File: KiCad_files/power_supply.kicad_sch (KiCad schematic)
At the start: 24 parts, among them Q2 DMP3099L, SW1 SLW-171175-7A-N-D, U7 LTC4412xS6

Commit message: comments
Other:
- note added: "Bootstrapping diode recommended by datasheet, since duty cycle expected be > 65% when powered through USB"
- note added: "DPDT switch because DPST switches with our power requirements were very expensive"
- note added: "Extra pad so that extra capacitor can be added if needed"
- note added: "Power LED"
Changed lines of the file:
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@@
 	(generator_version "9.0")
 	(paper "A4")
+	(text "Extra pad so that extra capacitor can be added if needed"
+		(exclude_from_sim no)
+		(at 198.374 123.19 0)
+		(effects
+			(font
+				(size 1.27 1.27)
+			)
+		)
+	)
 	(text "Power flags everywhere to tell ERC to STFU"
 		(exclude_from_sim no)
@@
 		(effects
 			(font
+				(size 1.27 1.27)
+			)
+		)
+	)
+	(text "Power LED"
+		(exclude_from_sim no)
+		(at 272.288 75.946 0)
+		(effects
+			(font
+				(size 1.27 1.27)
+			)
+		)
+	)
+	(text "Bootstrapping diode recommended by datasheet, since duty cycle expected be > 65% when powered through USB"
+		(exclude_from_sim no)
+		(at 192.278 31.242 0)
+		(effects
+			(font
+				(size 1.27 1.27)
+			)
+		)
+	)
+	(text "DPDT switch because DPST switches with our power requirements were very expensive"
+		(exclude_from_sim no)
+		(at 57.658 77.978 0)
+		(effects
+			(font

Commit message: more comments
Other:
- note added: "C25 and C26 are extra pad so that extra capacitor can be added if needed"
- note added: "LTC4412 is ideal diode. Uses reference design from datasheet"
- note added: "MP2235S is switching regulator (buck converter)"
- note added: "R11, C18, C19 and D3 form bootstrapping circuitry. 1n4148 diode recommended by datasheet when dutycycle > 65%"
- note added: "R12, R13, R14, C21 form feedback circuitry. From MPS DCDC-Designer tool"
- note added: "R15 is pullup resistor for BAT_STAT. LTC4412 pull down when current flows from USB"
- note added: "SW1 is power switch. Turns power on/off from both input power sources (USB and battery)"
- note removed: "Bootstrapping diode recommended by datasheet, since duty cycle expected be > 65% when powered through USB"
- note removed: "Extra pad so that extra capacitor can be added if needed"
- note removed: "Power flags everywhere to tell ERC to STFU"
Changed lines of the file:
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@@
 	(generator_version "9.0")
 	(paper "A4")
-	(text "Extra pad so that extra capacitor can be added if needed"
+	(text "C25 and C26 are extra pad so that extra capacitor can be added if needed"
 		(exclude_from_sim no)
-		(at 198.374 123.19 0)
+		(at 162.814 109.982 0)
 		(effects
 			(font
@@
 		)
 	)
-	(text "Power flags everywhere to tell ERC to STFU"
+	(text "SW1 is power switch. Turns power on/off from both input power sources (USB and battery)"
 		(exclude_from_sim no)
-		(at 68.58 69.596 0)
+		(at 58.166 53.848 0)
+		(effects
+			(font
+				(size 1.27 1.27)
+			)
+		)
+	)
+	(text "R12, R13, R14, C21 form feedback circuitry. From MPS DCDC-Designer tool"
+		(exclude_from_sim no)
+		(at 239.014 41.148 0)
+		(effects
+			(font
+				(size 1.27 1.27)
+			)
+		)
+	)
+	(text "R11, C18, C19 and D3 form bootstrapping circuitry. 1n4148 diode recommended by datasheet when dutycycle > 65%"
+		(exclude_from_sim no)
+		(at 166.37 32.766 0)
 		(effects
 			(font
@@
 		)
 	)
-	(text "Bootstrapping diode recommended by datasheet, since duty cycle expected be > 65% when powered through USB"
+	(text "R15 is pullup resistor for BAT_STAT. LTC4412 pull down when current flows from USB"
+		(exclude_from_sim no)
+		(at 235.712 148.082 0)
+		(effects
+			(font
+				(size 1.27 1.27)
+			)
+		)
+	)
+	(text "LTC4412 is ideal diode. Uses reference design from datasheet"
 		(exclude_from_sim no)
-		(at 192.278 31.242 0)
+		(at 67.564 164.846 0)
+		(effects
+			(font
+				(size 1.27 1.27)
+			)
+		)
+	)
+	(text "MP2235S is switching regulator (buck converter)"
+		(exclude_from_sim no)
+		(at 138.938 18.796 0)
 		(effects
 			(font
@@
 	(text "DPDT switch because DPST switches with our power requirements were very expensive"
 		(exclude_from_sim no)
-		(at 57.658 77.978 0)
+		(at 55.626 60.198 0)
 		(effects
 			(font
@@
 		)
 		(instances
-			(project ""
+			(project "esp"
 				(path "/186d5500-054c-4b47-a89c-85f6ce2abe33/718dca9f-314d-4628-afec-7956f3606013"
 					(reference "D1")
@@
 		)
 		(instances
-			(project ""
+			(project "esp"
 				(path "/186d5500-054c-4b47-a89c-85f6ce2abe33/718dca9f-314d-4628-afec-7956f3606013"
 					(reference "#PWR01")
@@
 		)
 		(instances
-			(project ""
+			(project "esp"
 				(path "/186d5500-054c-4b47-a89c-85f6ce2abe33/718dca9f-314d-4628-afec-7956f3606013"
 					(reference "#FLG04")
@@
 		)
 		(instances
-			(project ""
+			(project "esp"
 				(path "/186d5500-054c-4b47-a89c-85f6ce2abe33/718dca9f-314d-4628-afec-7956f3606013"
 					(reference "C20")
@@
 		)
 		(instances
-			(project ""
+			(project "esp"
 				(path "/186d5500-054c-4b47-a89c-85f6ce2abe33/718dca9f-314d-4628-afec-7956f3606013"
 					(reference "C21")
@@
 		)
 		(instances
-			(project ""
+			(project "esp"
 				(path "/186d5500-054c-4b47-a89c-85f6ce2abe33/718dca9f-314d-4628-afec-7956f3606013"
 					(reference "R15")
@@
 		)
 		(instances
-			(project ""
+			(project "esp"
 				(path "/186d5500-054c-4b47-a89c-85f6ce2abe33/718dca9f-314d-4628-afec-7956f3606013"
 					(reference "R1")
@@
 		)
 		(instances
-			(project ""
+			(project "esp"
 				(path "/186d5500-054c-4b47-a89c-85f6ce2abe33/718dca9f-314d-4628-afec-7956f3606013"
 					(reference "L4")
@@
 		)
 		(instances
-			(project ""
+			(project "esp"
 				(path "/186d5500-054c-4b47-a89c-85f6ce2abe33/718dca9f-314d-4628-afec-7956f3606013"
 					(reference "D3")
@@
 		)
 		(instances
-			(project ""
+			(project "esp"
 				(path "/186d5500-054c-4b47-a89c-85f6ce2abe33/718dca9f-314d-4628-afec-7956f3606013"
 					(reference "#PWR052")
@@
 		)
 		(instances
-			(project ""
+			(project "esp"
 				(path "/186d5500-054c-4b47-a89c-85f6ce2abe33/718dca9f-314d-4628-afec-7956f3606013"
 					(reference "#FLG07")
@@
 		)
 		(instances
-			(project ""
+			(project "esp"
 				(path "/186d5500-054c-4b47-a89c-85f6ce2abe33/718dca9f-314d-4628-afec-7956f3606013"
 					(reference "#PWR020")
@@
 		)
 		(instances
-			(project ""
+			(project "esp"
 				(path "/186d5500-054c-4b47-a89c-85f6ce2abe33/718dca9f-314d-4628-afec-7956f3606013"
 					(reference "SW1")

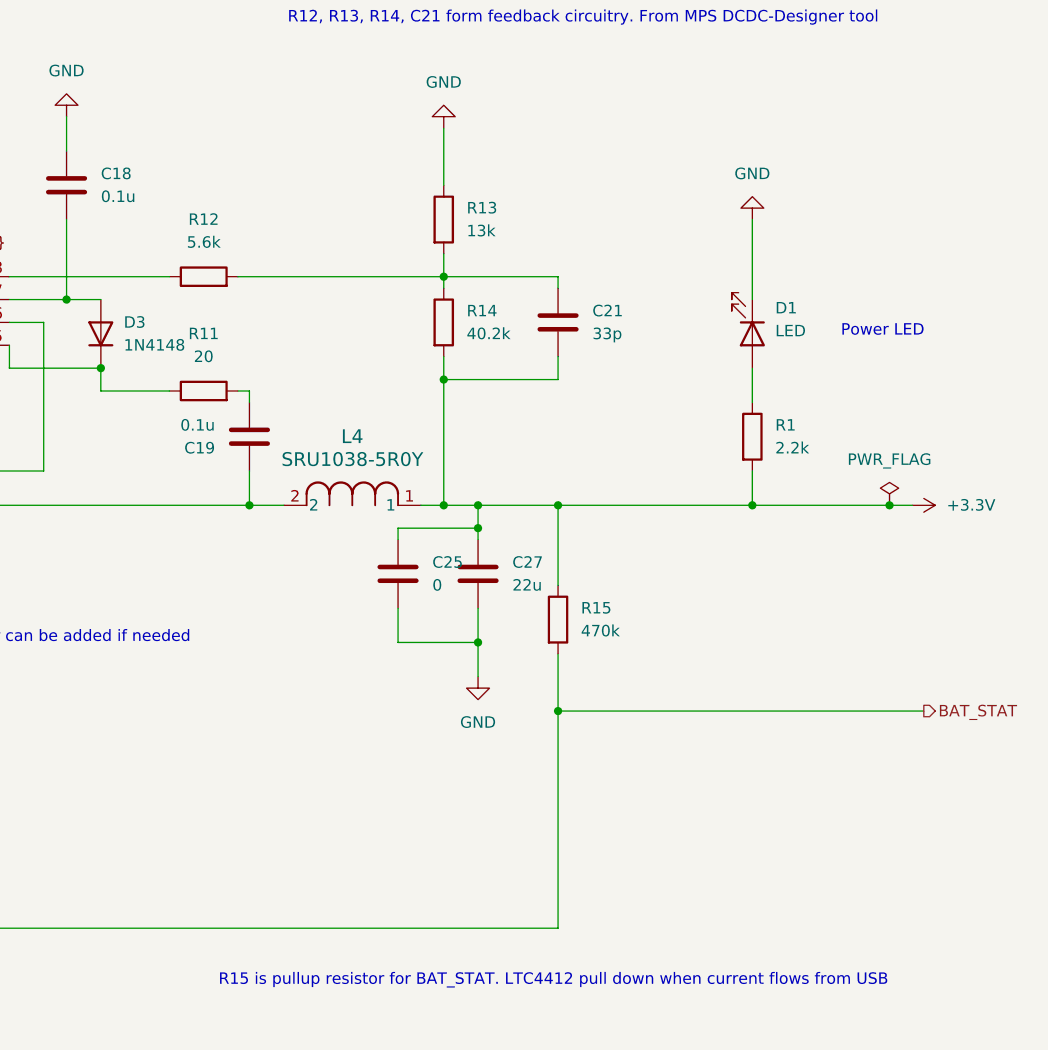
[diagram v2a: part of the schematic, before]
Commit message: jumper pins for disconnecting power supply
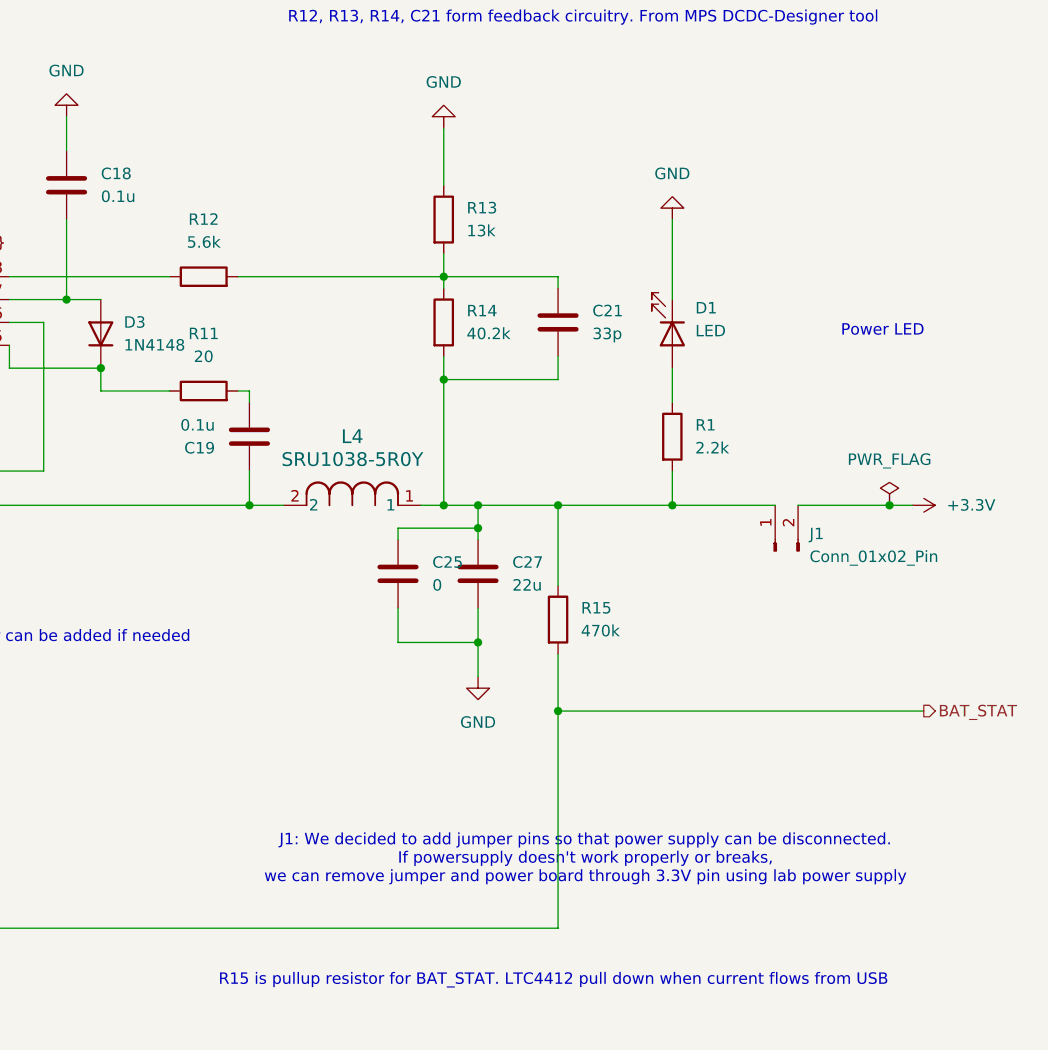
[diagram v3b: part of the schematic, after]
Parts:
- added J1: Conn_01x02_Pin, Connector_PinHeader_2.54mm:PinHeader_1x02_P2.54mm_Vertical, symbol Connector:Conn_01x02_Pin
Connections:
- net +3.3V: now also J1.2 (Pin_2); no longer C21.2, C25.1, C27.1, L4.1, R1.2, R14.2, R15.1
- new net: C21.2, C25.1, C27.1, J1.1 (Pin_1), L4.1, R1.2, R14.2, R15.1
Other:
- note added: "J1: We decided to add jumper pins so that power supply can be disconnected. If powersupply doesn't work properly or breaks, we can remove jumper and power board through 3.3V pin using lab power supply"
- moved on the sheet: D1, R1
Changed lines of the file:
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@@
+		)
+	)
+	(text "J1: We decided to add jumper pins so that power supply can be disconnected. \nIf powersupply doesn't work properly or breaks, \nwe can remove jumper and power board through 3.3V pin using lab power supply"
+		(exclude_from_sim no)
+		(at 239.268 134.62 0)
+		(effects
+			(font
+				(size 1.27 1.27)
+			)
 		)
 	)
@@
 	)
 	(junction
-		(at 257.81 95.25)
-		(diameter 0)
-		(color 0 0 0 0)
-	)
-	(junction
 		(at 39.37 72.39)
 		(diameter 0)
@@
 	)
 	(junction
-		(at 273.05 95.25)
-		(diameter 0)
-		(color 0 0 0 0)
-	)
-	(junction
 		(at 82.55 109.22)
 		(diameter 0)
@@
 	)
 	(junction
+		(at 273.05 95.25)
+		(diameter 0)
+		(color 0 0 0 0)
+	)
+	(junction
+		(at 248.92 95.25)
+		(diameter 0)
+		(color 0 0 0 0)
+	)
+	(junction
 		(at 124.46 72.39)
 		(diameter 0)
@@
 	(wire
 		(pts
-			(xy 257.81 63.5) (xy 257.81 72.39)
+			(xy 248.92 63.5) (xy 248.92 72.39)
 		)
 		(stroke
@@
 	(wire
 		(pts
+			(xy 262.89 95.25) (xy 273.05 95.25)
+		)
+		(stroke
+			(width 0)
+			(type default)
+		)
+	)
+	(wire
+		(pts
 			(xy 273.05 95.25) (xy 275.59 95.25)
 		)
@@
 	(wire
 		(pts
+			(xy 248.92 95.25) (xy 260.35 95.25)
+		)
+		(stroke
+			(width 0)
+			(type default)
+		)
+	)
+	(wire
+		(pts
 			(xy 201.93 95.25) (xy 205.74 95.25)
 		)
@@
 	(wire
 		(pts
-			(xy 257.81 80.01) (xy 257.81 83.82)
+			(xy 248.92 80.01) (xy 248.92 83.82)
 		)
 		(stroke
@@
 	(wire
 		(pts
-			(xy 257.81 95.25) (xy 273.05 95.25)
-		)
-		(stroke
-			(width 0)
-			(type default)
-		)
-	)
-	(wire
-		(pts
-			(xy 257.81 91.44) (xy 257.81 95.25)
+			(xy 248.92 91.44) (xy 248.92 95.25)
 		)
 		(stroke
@@
 	(wire
 		(pts
-			(xy 236.22 95.25) (xy 257.81 95.25)
+			(xy 236.22 95.25) (xy 248.92 95.25)
 		)
 		(stroke
@@
 	(symbol
 		(lib_id "Device:LED")
-		(at 257.81 76.2 270)
+		(at 248.92 76.2 270)
 		(unit 1)
 		(exclude_from_sim no)
@@
 		(fields_autoplaced yes)
 		(property "Reference" "D1"
-			(at 260.35 73.3424 90)
+			(at 251.46 73.3424 90)
 			(effects
 				(font
@@
 		)
 		(property "Value" "LED"
-			(at 260.35 75.8824 90)
+			(at 251.46 75.8824 90)
 			(effects
 				(font
@@
 		)
 		(property "Footprint" "LED_SMD:LED_0805_2012Metric_Pad1.15x1.40mm_HandSolder"
-			(at 257.81 76.2 0)
+			(at 248.92 76.2 0)
 			(effects
 				(font
@@
 		)
 		(property "Datasheet" "~"
-			(at 257.81 76.2 0)
+			(at 248.92 76.2 0)
 			(effects
 				(font
@@
 		)
 		(property "Description" "Light emitting diode"
-			(at 257.81 76.2 0)
+			(at 248.92 76.2 0)
 			(effects
 				(font
@@
 		)
 		(property "Sim.Pins" "1=K 2=A"
-			(at 257.81 76.2 0)
+			(at 248.92 76.2 0)
 			(effects
 				(font
@@
 		)
 		(property "DigiKey" "492-2281-1-ND"
-			(at 257.81 76.2 90)
+			(at 248.92 76.2 90)
 			(effects
 				(font
@@
 		)
 		(property "MNF PART NUMBER" ""
-			(at 257.81 76.2 90)
+			(at 248.92 76.2 90)
 			(effects
 				(font
@@
 		)
 		(property "Sim.Type" ""
-			(at 257.81 76.2 90)
+			(at 248.92 76.2 90)
 			(effects
 				(font
@@
 	(symbol
 		(lib_id "power:GND")
-		(at 257.81 63.5 180)
+		(at 248.92 63.5 180)
 		(unit 1)
 		(exclude_from_sim no)
@@
 		(fields_autoplaced yes)
 		(property "Reference" "#PWR01"
-			(at 257.81 57.15 0)
+			(at 248.92 57.15 0)
 			(effects
 				(font
@@
 		)
 		(property "Value" "GND"
-			(at 257.81 58.42 0)
+			(at 248.92 58.42 0)
 			(effects
 				(font
@@
 		)
 		(property "Footprint" ""
-			(at 257.81 63.5 0)
+			(at 248.92 63.5 0)
 			(effects
 				(font
@@
 		)
 		(property "Datasheet" ""
-			(at 257.81 63.5 0)
+			(at 248.92 63.5 0)
 			(effects
 				(font
@@
 		)
 		(property "Description" "Power symbol creates a global label with name \"GND\" , ground"
-			(at 257.81 63.5 0)
+			(at 248.92 63.5 0)
 			(effects
 				(font
@@
 	(symbol
 		(lib_id "Device:R")
-		(at 257.81 87.63 0)
+		(at 248.92 87.63 0)
 		(unit 1)
 		(exclude_from_sim no)
@@
 		(fields_autoplaced yes)
 		(property "Reference" "R1"
-			(at 260.35 86.3599 0)
+			(at 251.46 86.3599 0)
 			(effects
 				(font
@@
 		)
 		(property "Value" "2.2k"
-			(at 260.35 88.8999 0)
+			(at 251.46 88.8999 0)
 			(effects
 				(font
@@
 		)
 		(property "Footprint" "Resistor_SMD:R_0805_2012Metric_Pad1.20x1.40mm_HandSolder"
-			(at 256.032 87.63 90)
+			(at 247.142 87.63 90)
 			(effects
 				(font
@@
 		)
 		(property "Datasheet" "~"
-			(at 257.81 87.63 0)
+			(at 248.92 87.63 0)
 			(effects
 				(font
@@
 		)
 		(property "Description" "Resistor"
-			(at 257.81 87.63 0)
+			(at 248.92 87.63 0)
 			(effects
 				(font
@@
 		)
 		(property "DigiKey" "311-2.20KCRCT-ND"
-			(at 257.81 87.63 0)
+			(at 248.92 87.63 0)
 			(effects
 				(font
@@
 		)
 		(property "MNF PART NUMBER" ""
-			(at 257.81 87.63 0)
+			(at 248.92 87.63 0)
 			(effects
 				(font
@@
 		)
 		(property "Sim.Type" ""
-			(at 257.81 87.63 0)
+			(at 248.92 87.63 0)
 			(effects
 				(font
@@
 					(unit 1)
 				)
+			)
+		)
+	)
+	(symbol
+		(lib_id "Connector:Conn_01x02_Pin")
+		(at 260.35 100.33 90)
+		(unit 1)
+		(exclude_from_sim no)
+		(in_bom yes)
+		(on_board yes)
+		(dnp no)
+		(fields_autoplaced yes)
+		(property "Reference" "J1"
+			(at 264.16 98.4249 90)
+			(effects
+				(font
+					(size 1.27 1.27)
+				)
+				(justify right)
+			)
+		)
+		(property "Value" "Conn_01x02_Pin"
+			(at 264.16 100.9649 90)
+			(effects
+				(font
+					(size 1.27 1.27)
+				)
+				(justify right)
+			)
+		)
+		(property "Footprint" "Connector_PinHeader_2.54mm:PinHeader_1x02_P2.54mm_Vertical"
+			(at 260.35 100.33 0)
+			(effects
+				(font
+					(size 1.27 1.27)
+				)
+				(hide yes)
+			)
+		)
+		(property "Datasheet" "~"
+			(at 260.35 100.33 0)
+			(effects
+				(font
+					(size 1.27 1.27)
+				)
+				(hide yes)
+			)
+		)
+		(property "Description" "Generic connector, single row, 01x02, script generated"
+			(at 260.35 100.33 0)
+			(effects
+				(font
+					(size 1.27 1.27)
+				)
+				(hide yes)
+			)
+		)
+		(pin "2"
+		)
+		(pin "1"
+		)
+		(instances
+			(project "esp"
+				(path "/186d5500-054c-4b47-a89c-85f6ce2abe33/718dca9f-314d-4628-afec-7956f3606013"
+					(reference "J1")
+					(unit 1)
+				)
